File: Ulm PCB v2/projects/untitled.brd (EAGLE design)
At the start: 56.6 x 49.2 mm, 27 parts, among them U1 FT232RLSSOP, U2 MCP73831, U3 SPX3819-3.3, U4 RFM69HCW, X2 USB-SMD-NS

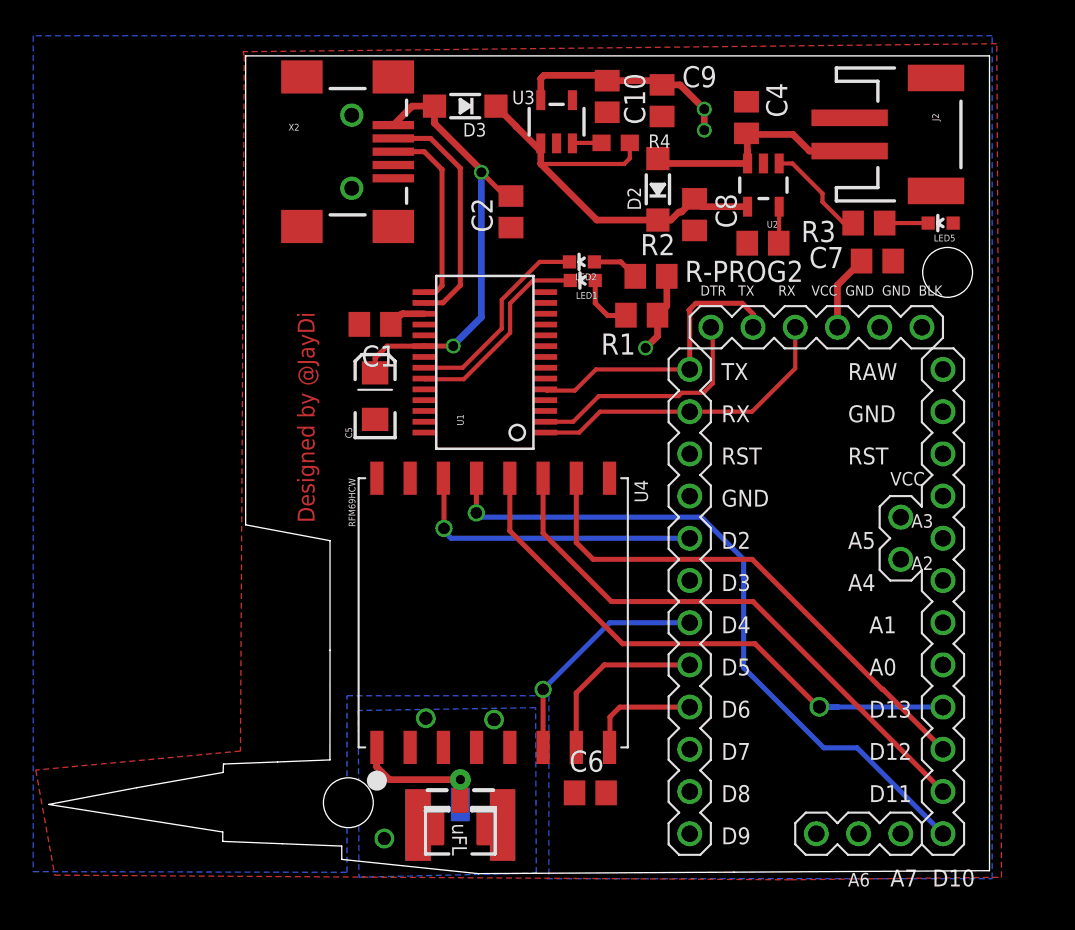
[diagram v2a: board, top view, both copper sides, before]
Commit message: Fixed Cap. Values for better voltage stabilazation
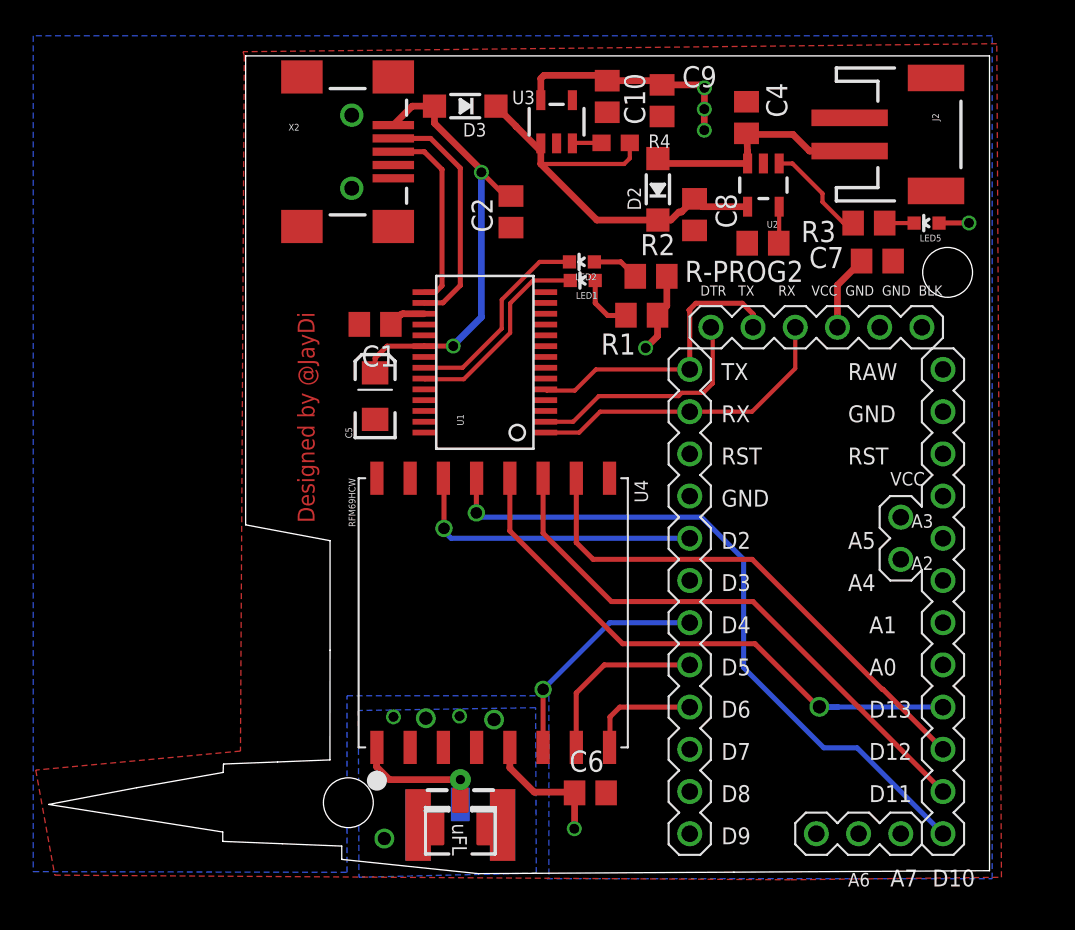
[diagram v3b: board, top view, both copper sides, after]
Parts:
- moved LED5 0.85 mm to (53.8, 40.4)
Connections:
- removed net +3V3: LED5.A
- removed net N$16: U4.2P
- removed net VCC: U4.5P
- net 3.3V: now also C6.1, LED5.A, U4.5P
- net GND: now also U4.2P
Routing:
- net 3.3V: track 23.3 -> 33.8 mm, vias 3 -> 6
- net N$5: track 2.62 -> 1.77 mm
- net GND: vias 3 -> 5
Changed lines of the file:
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@@
 <attribute name="VALUE" x="43.2816" y="36.6354375" size="1.27" layer="27"/>
 </element>
-<element name="LED5" library="SparkFun" package="LED-0603" value="Green" x="54.61" y="40.386" rot="R90"/>
+<element name="LED5" library="SparkFun" package="LED-0603" value="Green" x="53.763165625" y="40.386" rot="R90"/>
 <element name="J2" library="SparkFun-Connectors" package="JST-2-SMD" value="" x="52.832" y="45.72" rot="R270">
 <attribute name="PROD_ID" value="CONN-08352" x="69.088" y="54.61" size="1.778" layer="27" rot="R270" display="off"/>
@@
 <via x="27.733878125" y="10.500765625" extent="1-16" drill="0.8"/>
 <via x="21.128559375" y="3.345003125" extent="1-16" drill="0.8"/>
+<via x="21.679003125" y="10.670134375" extent="1-16" drill="0.6"/>
+<via x="25.65913125" y="10.712475" extent="1-16" drill="0.6"/>
+<contactref element="U4" pad="2P"/>
 </signal>
 <signal name="USB_D-">
@@
 <contactref element="R1" pad="2"/>
 <wire x1="49.596" y1="37.846" x2="49.85" y2="38.1" width="0.4064" layer="1"/>
-<wire x1="37.846" y1="48.702" x2="38.928" y2="48.702" width="0.4064" layer="1"/>
-<wire x1="38.928" y1="48.702" x2="40.386" y2="47.244" width="0.4064" layer="1"/>
 <wire x1="40.386" y1="47.244" x2="40.386" y2="45.974" width="0.4064" layer="1"/>
 <via x="40.386" y="47.244" extent="1-16" drill="0.6"/>
@@
 <wire x1="37.57105" y1="34.84124375" x2="37.57105" y2="33.58325" width="0.4064" layer="1"/>
 <wire x1="37.57105" y1="33.58325" x2="36.8554" y2="32.8676" width="0.4064" layer="1"/>
-<wire x1="36.83" y1="32.8422" x2="36.8554" y2="32.8676" width="0.4064" layer="1"/>
 <wire x1="36.8554" y1="32.8676" x2="36.83" y2="32.8422" width="0.4064" layer="1"/>
 <via x="36.8554" y="32.8676" extent="1-16" drill="0.6" diameter="0.85"/>
@@
 <vertex x="31.036540625" y="0.9738625"/>
 </polygon>
+<contactref element="LED5" pad="A"/>
+<via x="56.31459375" y="40.394078125" extent="1-16" drill="0.6"/>
+<wire x1="56.31459375" y1="40.394078125" x2="54.52124375" y2="40.394078125" width="0.3048" layer="1"/>
+<wire x1="54.52124375" y1="40.394078125" x2="54.513165625" y2="40.386" width="0.3048" layer="1"/>
+<via x="40.394078125" y="48.523703125" extent="1-16" drill="0.6"/>
+<wire x1="40.21578125" y1="48.702" x2="40.394078125" y2="48.523703125" width="0.4064" layer="1"/>
+<wire x1="37.846" y1="48.702" x2="40.21578125" y2="48.702" width="0.4064" layer="1"/>
+<wire x1="40.394078125" y1="48.523703125" x2="40.394078125" y2="47.252078125" width="0.4064" layer="1"/>
+<wire x1="40.394078125" y1="47.252078125" x2="40.386" y2="47.244" width="0.4064" layer="1"/>
+<contactref element="U4" pad="5P"/>
+<contactref element="C6" pad="1"/>
+<wire x1="28.683234375" y1="8.8316375" x2="28.683234375" y2="7.603690625" width="0.4064" layer="1"/>
+<wire x1="28.683234375" y1="7.603690625" x2="30.1473625" y2="6.1395625" width="0.4064" layer="1"/>
+<wire x1="30.1473625" y1="6.1395625" x2="32.5344375" y2="6.1395625" width="0.4064" layer="1"/>
+<wire x1="32.5344375" y1="6.1395625" x2="32.578" y2="6.096" width="0.4064" layer="1"/>
+<wire x1="32.578" y1="6.096" x2="32.578" y2="4.166653125" width="0.4064" layer="1"/>
+<wire x1="32.578" y1="4.166653125" x2="32.56084375" y2="4.149496875" width="0.4064" layer="1"/>
+<wire x1="32.56084375" y1="4.149496875" x2="32.56084375" y2="3.9377875" width="0.4064" layer="1"/>
+<via x="32.56084375" y="3.9377875" extent="1-16" drill="0.6"/>
 </signal>
 <signal name="TXLED">
@@
 <contactref element="LED5" pad="C"/>
 <contactref element="R3" pad="1"/>
-<wire x1="51.242" y1="40.386" x2="53.86" y2="40.386" width="0.254" layer="1"/>
+<wire x1="51.242" y1="40.386" x2="53.013165625" y2="40.386" width="0.254" layer="1"/>
 </signal>
 <signal name="D7">
@@
 <wire x1="22.08860625" y1="34.85460625" x2="21.524" y2="34.29" width="0.4064" layer="1"/>
 </signal>
-<signal name="+3V3">
-<contactref element="LED5" pad="A"/>
-</signal>
-<signal name="N$16">
-<contactref element="U4" pad="2P"/>
-</signal>
-<signal name="VCC">
-<contactref element="U4" pad="5P"/>
-</signal>
 <signal name="D2">

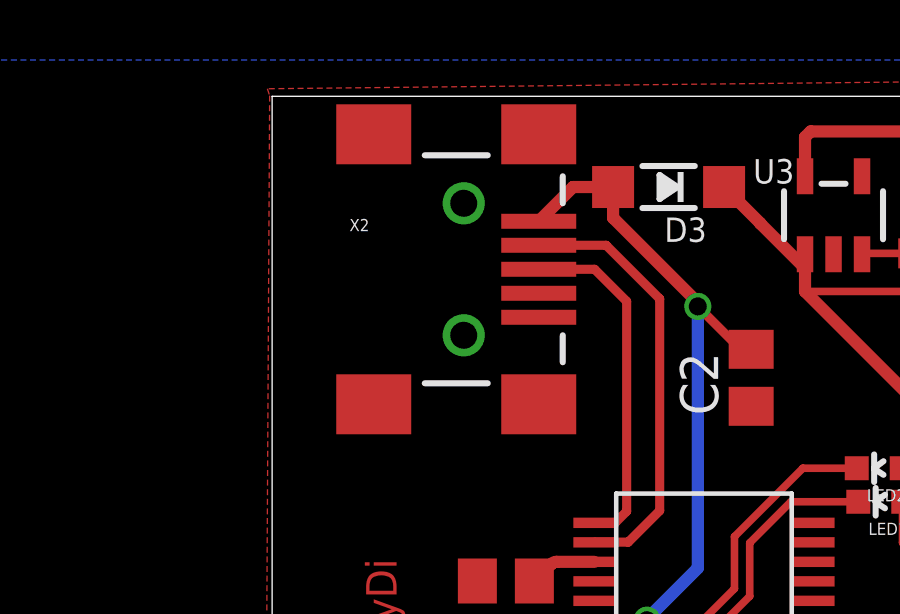
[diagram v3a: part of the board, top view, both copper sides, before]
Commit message: added microUSB
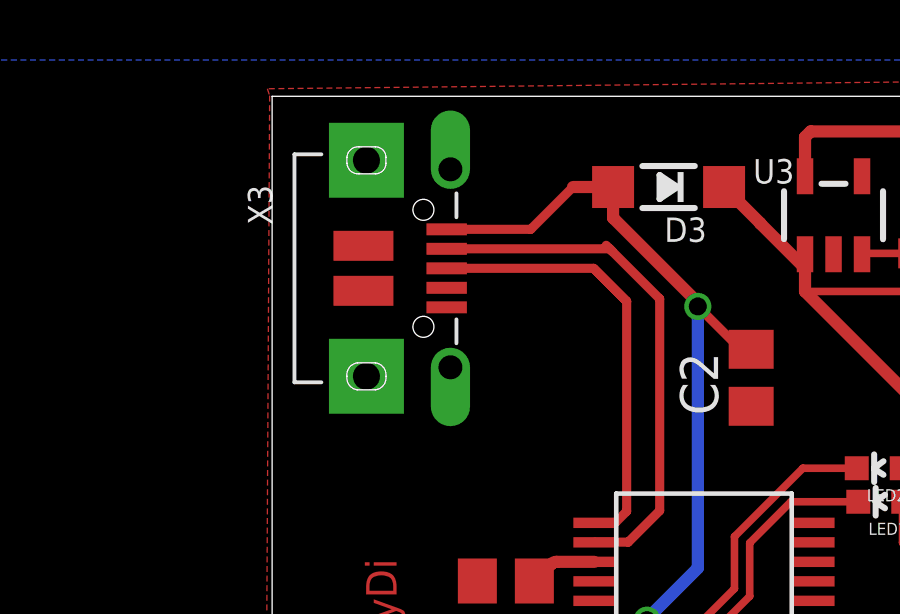
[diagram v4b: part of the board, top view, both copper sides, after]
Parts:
- removed X2: USB-SMD-NS, SparkFun:USB-MINIB-NOSTOP
- added X3: microUSB, microbuilder:4UCONN_20329_V2
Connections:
- net GND: now also X3.BASE@1, X3.BASE@2, X3.GND, X3.SPRT@1, X3.SPRT@2, X3.SPRT@3, X3.SPRT@4; no longer X2.GND
- net USB_D+: now also X3.D+; no longer X2.D+
- net USB_D-: now also X3.D-; no longer X2.D-
- net VBUS: now also X3.VBUS; no longer X2.VBUS
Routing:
- net USB_D+: track 11.7 -> 16.2 mm
- net USB_D-: track 14.5 -> 17.8 mm
- net VBUS: track 27.8 -> 31.0 mm
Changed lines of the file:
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@@
 <element name="U$1" library="arduinopromini" package="ARDUINO_PRO_MINI" value="" x="43.3194625" y="22.68590625"/>
 <element name="U1" library="SparkFun" package="SSOP28DB" value="FT232RLSSOP" x="27.178" y="32.004" rot="R90"/>
-<element name="X2" library="SparkFun" package="USB-MINIB-NOSTOP" value="USB-SMD-NS" x="19.169625" y="44.680746875"/>
 <element name="U2" library="SparkFun-PowerIC" package="SOT23-5" value="MCP73831" x="43.942" y="42.672" rot="R180">
 <attribute name="PROD_ID" value="IC-09995" x="47.244" y="-18.034" size="1.778" layer="27" rot="R180" display="off"/>
@@
 <element name="U4" library="microbuilder" package="RFMHCW_SMT" value="RFM69HCW" x="27.683234375" y="16.9316375" rot="R270"/>
 <element name="D3" library="microbuilder" package="SOD-123" value="MBR120" x="25.997865625" y="47.422815625" rot="R180"/>
+<element name="X3" library="microbuilder" package="4UCONN_20329_V2" value="microUSB" x="17.825896875" y="44.712940625" rot="R270"/>
 </elements>
 <signals>
 <signal name="GND">
 <contactref element="C1" pad="2"/>
-<contactref element="X2" pad="GND"/>
 <contactref element="U1" pad="26"/>
 <contactref element="U1" pad="25"/>
@@
 <via x="25.65913125" y="10.712475" extent="1-16" drill="0.6"/>
 <contactref element="U4" pad="2P"/>
+<contactref element="X3" pad="BASE@2"/>
+<contactref element="X3" pad="BASE@1"/>
+<contactref element="X3" pad="GND"/>
+<contactref element="X3" pad="SPRT@2"/>
+<contactref element="X3" pad="SPRT@3"/>
+<contactref element="X3" pad="SPRT@4"/>
+<contactref element="X3" pad="SPRT@1"/>
 </signal>
 <signal name="USB_D-">
-<contactref element="X2" pad="D-"/>
 <contactref element="U1" pad="16"/>
 <wire x1="23.522" y1="35.579" x2="23.503" y2="35.56" width="0.254" layer="1"/>
 <wire x1="24.653065625" y1="35.5854" x2="23.53745" y2="35.5854" width="0.3048" layer="1"/>
 <wire x1="23.53745" y1="35.5854" x2="23.522" y2="35.579" width="0.3048" layer="1" curve="45"/>
-<wire x1="21.669625" y1="45.480746875" x2="23.9174625" y2="45.480746875" width="0.3048" layer="1"/>
-<wire x1="23.9174625" y1="45.480746875" x2="25.701471875" y2="43.6967375" width="0.3048" layer="1"/>
+<wire x1="24.12000625" y1="45.278203125" x2="23.9174625" y2="45.480746875" width="0.3048" layer="1"/>
+<wire x1="24.12000625" y1="45.278203125" x2="25.701471875" y2="43.6967375" width="0.3048" layer="1"/>
 <wire x1="25.701471875" y1="43.6967375" x2="25.701471875" y2="36.63380625" width="0.3048" layer="1"/>
 <wire x1="25.701471875" y1="36.63380625" x2="24.653065625" y2="35.5854" width="0.3048" layer="1"/>
+<contactref element="X3" pad="D-"/>
+<wire x1="18.600896875" y1="45.362940625" x2="24.03526875" y2="45.362940625" width="0.3048" layer="1"/>
+<wire x1="24.03526875" y1="45.362940625" x2="24.12000625" y2="45.278203125" width="0.3048" layer="1"/>
 </signal>
 <signal name="USB_D+">
-<contactref element="X2" pad="D+"/>
 <contactref element="U1" pad="15"/>
 <wire x1="24.216559375" y1="36.229" x2="23.522" y2="36.229" width="0.3048" layer="1"/>
-<wire x1="21.674809375" y1="44.7294" x2="21.669625" y2="44.680746875" width="0.3048" layer="1" curve="-45"/>
-<wire x1="21.669625" y1="44.680746875" x2="23.531890625" y2="44.680746875" width="0.3048" layer="1"/>
-<wire x1="23.531890625" y1="44.680746875" x2="24.600584375" y2="43.612053125" width="0.3048" layer="1"/>
+<wire x1="24.600584375" y1="43.612053125" x2="23.531890625" y2="44.680746875" width="0.3048" layer="1"/>
 <wire x1="24.600584375" y1="43.612053125" x2="24.600584375" y2="36.613025" width="0.3048" layer="1"/>
 <wire x1="24.600584375" y1="36.613025" x2="24.216559375" y2="36.229" width="0.3048" layer="1"/>
+<contactref element="X3" pad="D+"/>
+<wire x1="18.600896875" y1="44.712940625" x2="23.499696875" y2="44.712940625" width="0.3048" layer="1"/>
+<wire x1="23.499696875" y1="44.712940625" x2="24.600584375" y2="43.612053125" width="0.3048" layer="1"/>
 </signal>
 <signal name="CTS">
@@
 <contactref element="C5" pad="A"/>
 <contactref element="C2" pad="1"/>
-<contactref element="X2" pad="VBUS"/>
 <wire x1="20.574" y1="31.372" x2="20.657" y2="31.455" width="0.254" layer="1"/>
 <wire x1="21.295" y1="32.979" x2="20.574" y2="32.258" width="0.3048" layer="1"/>
@@
 <contactref element="D3" pad="A"/>
 <wire x1="22.81169375" y1="47.422815625" x2="24.147865625" y2="47.422815625" width="0.4064" layer="1"/>
-<wire x1="21.669625" y1="46.280746875" x2="22.81169375" y2="47.422815625" width="0.4064" layer="1"/>
 <wire x1="24.147865625" y1="47.422815625" x2="24.147865625" y2="46.393571875" width="0.4064" layer="1"/>
 <wire x1="27.056409375" y1="43.485028125" x2="27.01406875" y2="43.485028125" width="0.4064" layer="1"/>
@@
 <wire x1="28.75131875" y1="42.013496875" x2="28.40091875" y2="42.013496875" width="0.3048" layer="1"/>
 <wire x1="28.40091875" y1="42.013496875" x2="26.971728125" y2="43.4426875" width="0.3048" layer="1"/>
+<contactref element="X3" pad="VBUS"/>
+<wire x1="18.600896875" y1="46.012940625" x2="21.40181875" y2="46.012940625" width="0.3048" layer="1"/>
+<wire x1="21.40181875" y1="46.012940625" x2="22.81169375" y2="47.422815625" width="0.3048" layer="1"/>
 </signal>
 <signal name="V5">
